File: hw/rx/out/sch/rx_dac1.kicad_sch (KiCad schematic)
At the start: 14 parts, among them U3 PCM5102A

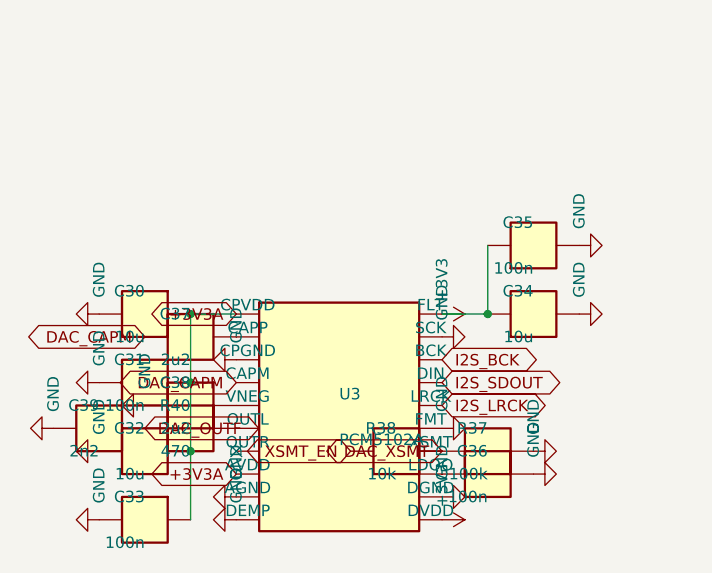
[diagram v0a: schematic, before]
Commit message: hw/rx: BT40E + TQ2SA footprints, THT underside backplane header, bring-up test points (#34)
Co-Authored-By: Claude Opus 5.5 <noreply@anthropic.com>
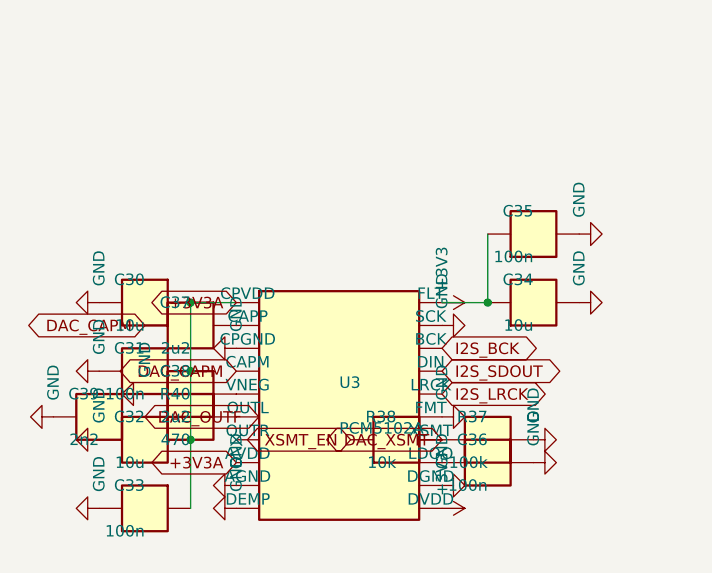
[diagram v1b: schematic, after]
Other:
- moved on the sheet: C30, C31, C32, C33, C34, C35, C36, C37, C38, C39, R37, R38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

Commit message: hw/rx + hw/pack: #116 review fixes: netclass pour clearances (no 0.09 mm override), keyed J1 with no hole at 14, solid RF grounds, K1 pin-1/CPL rotation, raw RF numbers (#34)
- M1: JLC copper-clearance rule removed from rx and pack .kicad_dru; boards refilled/regenerated; probe-rule tests
  assert >= 0.125 mm everywhere and >= 0.15 mm to Audio_I on the committed fill; outer-copper rule width-independent
- S1: openpack:PinHeader_2x13_P2.54mm_Key14 (pad 14 deleted, KEY silk), header XFCN PZ254V-12-26P (LCSC C22465887,
  pin 14 cut), main-board socket Samtec SSW-113-01-G-D-14 recorded in ADR-0014; test
- S2: zone_connect solid on J3-J5, U2, U1 GND pads; test
- S3: TQ2SA pin-1 dot + '+', CPL +270 for the relay (K1 at 180); pin-1 marker + CPL test for all polarized parts
- N1 raw RF Z0 (51.5 bare / ~49.3 masked), N3 C44 at U6, REVIEW follow-ups

Co-Authored-By: Claude Opus 5.5 <noreply@anthropic.com>
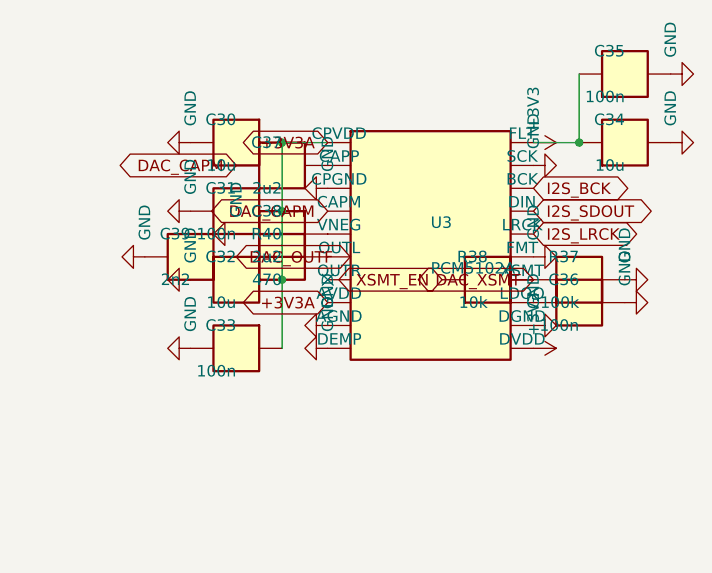
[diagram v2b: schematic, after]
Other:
- moved on the sheet: C30, C31, C32, C33, C34, C35, C36, C37, C38, C39, R37, R38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
